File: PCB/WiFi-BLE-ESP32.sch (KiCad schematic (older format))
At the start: 12 parts

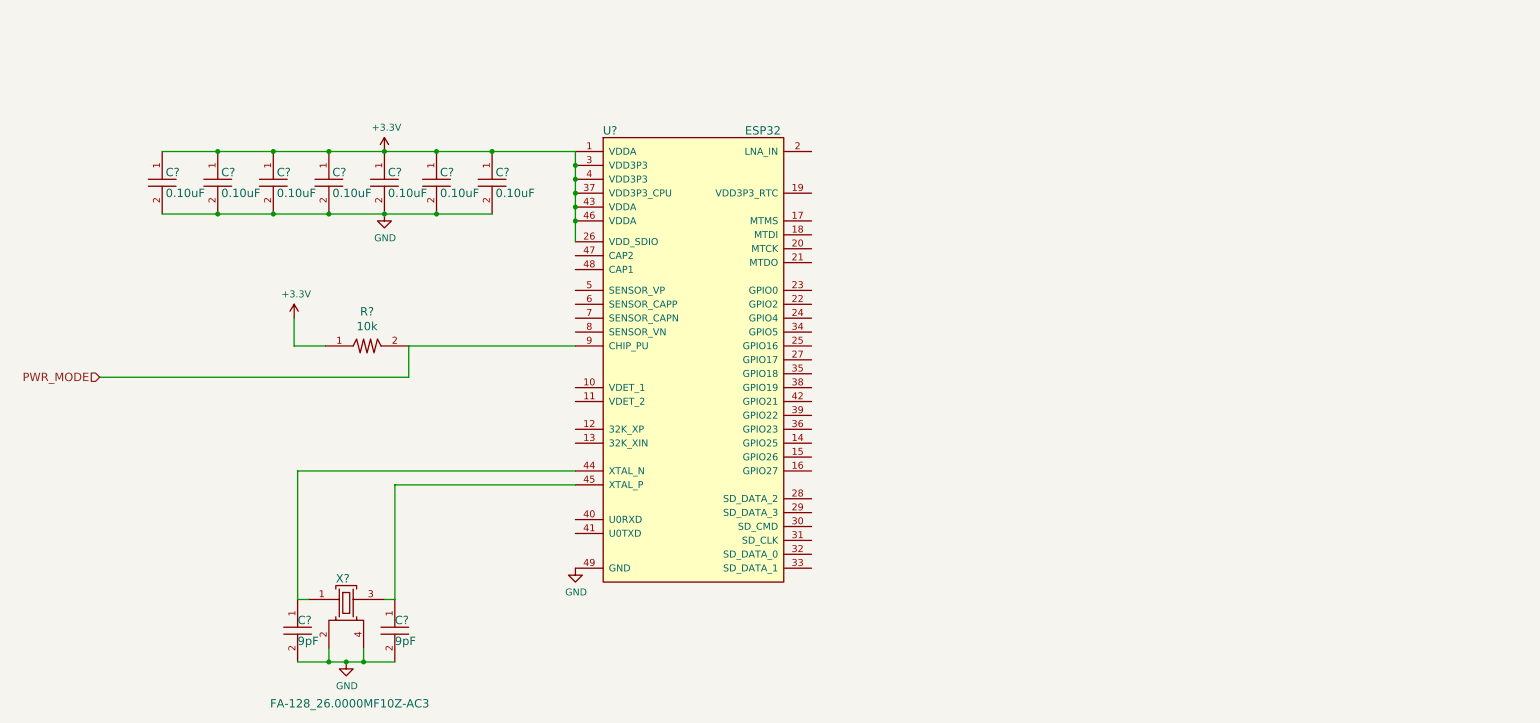
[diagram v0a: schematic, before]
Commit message: Schematic Done, Board Underway
Schematic completed. STM32 section upated from Aria project schematic,
ESP32 schematic completed with the help of reference schematic.
Datasheets for componens used also added. The PCB is near complete, Aria
was improted and modifed to speed up the process. More to come!
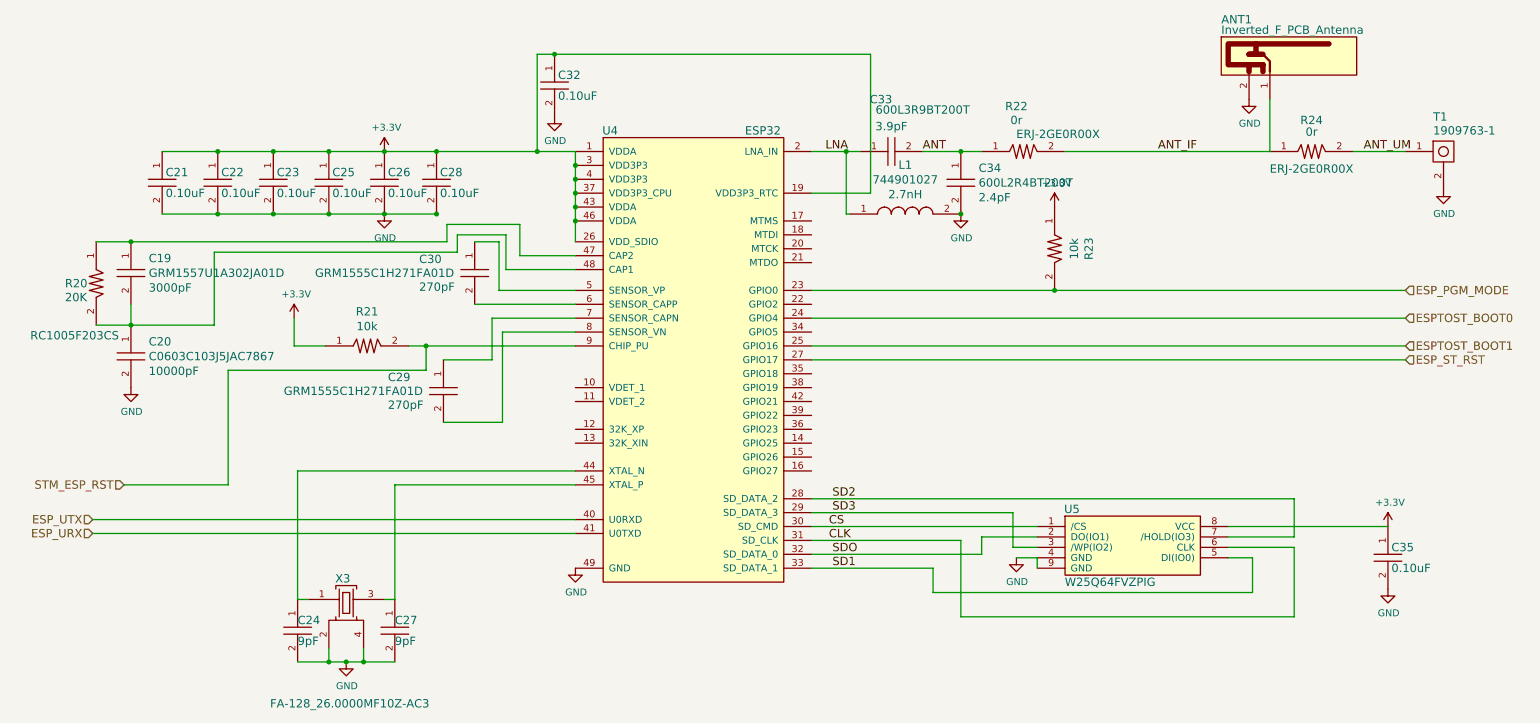
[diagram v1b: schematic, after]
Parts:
- removed C?: CL05B104JP5NNNC, PCB_Footprints:C0402, symbol CL05B104JP5NNNC
- added ANT1: Inverted_F_PCB_Antenna, PCB_Footprints:PCB_IF_ANT_2.4G, symbol Inverted_F_PCB_Antenna
- added C19: GRM1557U1A302JA01D, PCB_Footprints:C0402, symbol GRM1557U1A302JA01D
- added C20: C0603C103J5JAC7867, PCB_Footprints:C0603, symbol C0603C103J5JAC7867
- added C29, C30: GRM1555C1H271FA01D, PCB_Footprints:C0402, symbol GRM1555C1H271FA01D
- added C32, C35: CL05B104JP5NNNC, PCB_Footprints:C0402, symbol CL05B104JP5NNNC
- added C33: 600L3R9BT200T, PCB_Footprints:C0402, symbol 600L3R9BT200T
- added C34: 600L2R4BT200T, PCB_Footprints:C0402, symbol 600L2R4BT200T
- added L1: 744901027, PCB_Footprints:BLM15HG601SN1D, symbol 744901027
- added R20: RC1005F203CS, PCB_Footprints:R0402, symbol RC1005F203CS
- added R22, R24: ERJ-2GE0R00X, PCB_Footprints:R0402, symbol ERJ-2GE0R00X
- added R23: RC1005F103CS, PCB_Footprints:R0402, symbol RC1005F103CS
- added T1: 1909763-1, PCB_Footprints:1909763-1, symbol 1909763-1
- added U5: W25Q64FVZPIG, PCB_Footprints:W25Q64FVZPIG, symbol W25Q64FVZPIG
- gave numbers to parts that had none: 11
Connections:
- net +3V3: now also U4.19 (VDD3P3_RTC), C32.1, C35.1, R23.1, U5.8 (VCC)
- net GND: now also ANT1.2, C20.2, C32.2, C34.2, C35.2, L1.2, T1.2, U5.4 (GND), U5.9 (GND)
- net LNA: now reaches U4.2 (LNA_IN)
- net LNA: now also C33.1, L1.1
- net ESP_PGM_MODE: now reaches U4.23 (GPIO0)
- net ESP_PGM_MODE: now also R23.2
- net ESPTOST_BOOT0: now reaches U4.24 (GPIO4)
- net ESPTOST_BOOT1: now reaches U4.25 (GPIO16)
- net ESP_ST_RST: now reaches U4.27 (GPIO17)
- net SD2: now reaches U4.28 (SD_DATA_2)
- net SD2: now also U5.7 (/HOLD(IO3))
- net SD3: now reaches U4.29 (SD_DATA_3)
- net SD3: now also U5.3 (/WP(IO2))
- net CS: now reaches U4.30 (SD_CMD)
- net CS: now also U5.1 (/CS)
- net CLK: now reaches U4.31 (SD_CLK)
- net CLK: now also U5.6 (CLK)
- net SDO: now reaches U4.32 (SD_DATA_0)
- net SDO: now also U5.2 (DO(IO1))
- net SD1: now reaches U4.33 (SD_DATA_1)
- net SD1: now also U5.5 (DI(IO0))
- net ESP_UTX: now reaches U4.40 (U0RXD)
- net ESP_URX: now reaches U4.41 (U0TXD)
- net at U4.47 (CAP2): now also C19.1, R20.1
- net at U4.48 (CAP1): now also C19.2, C20.1, R20.2
- net at U4.5 (SENSOR_VP): now also C30.1
- net at U4.6 (SENSOR_CAPP): now also C30.2
- net at U4.7 (SENSOR_CAPN): now also C29.1
- net at U4.8 (SENSOR_VN): now also C29.2
- net PWR_MODE renamed STM_ESP_RST
- new net ANT: C33.2, C34.1, R22.1
- new net ANT_IF: ANT1.1, R22.2, R24.1
- new net ANT_UM: R24.2, T1.1
